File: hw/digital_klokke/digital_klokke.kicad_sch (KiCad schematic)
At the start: 8 parts, among them J101 Conn_01x02_Pin, SW101 SW_Push, SW102 SW_Push, SW103 SW_Push

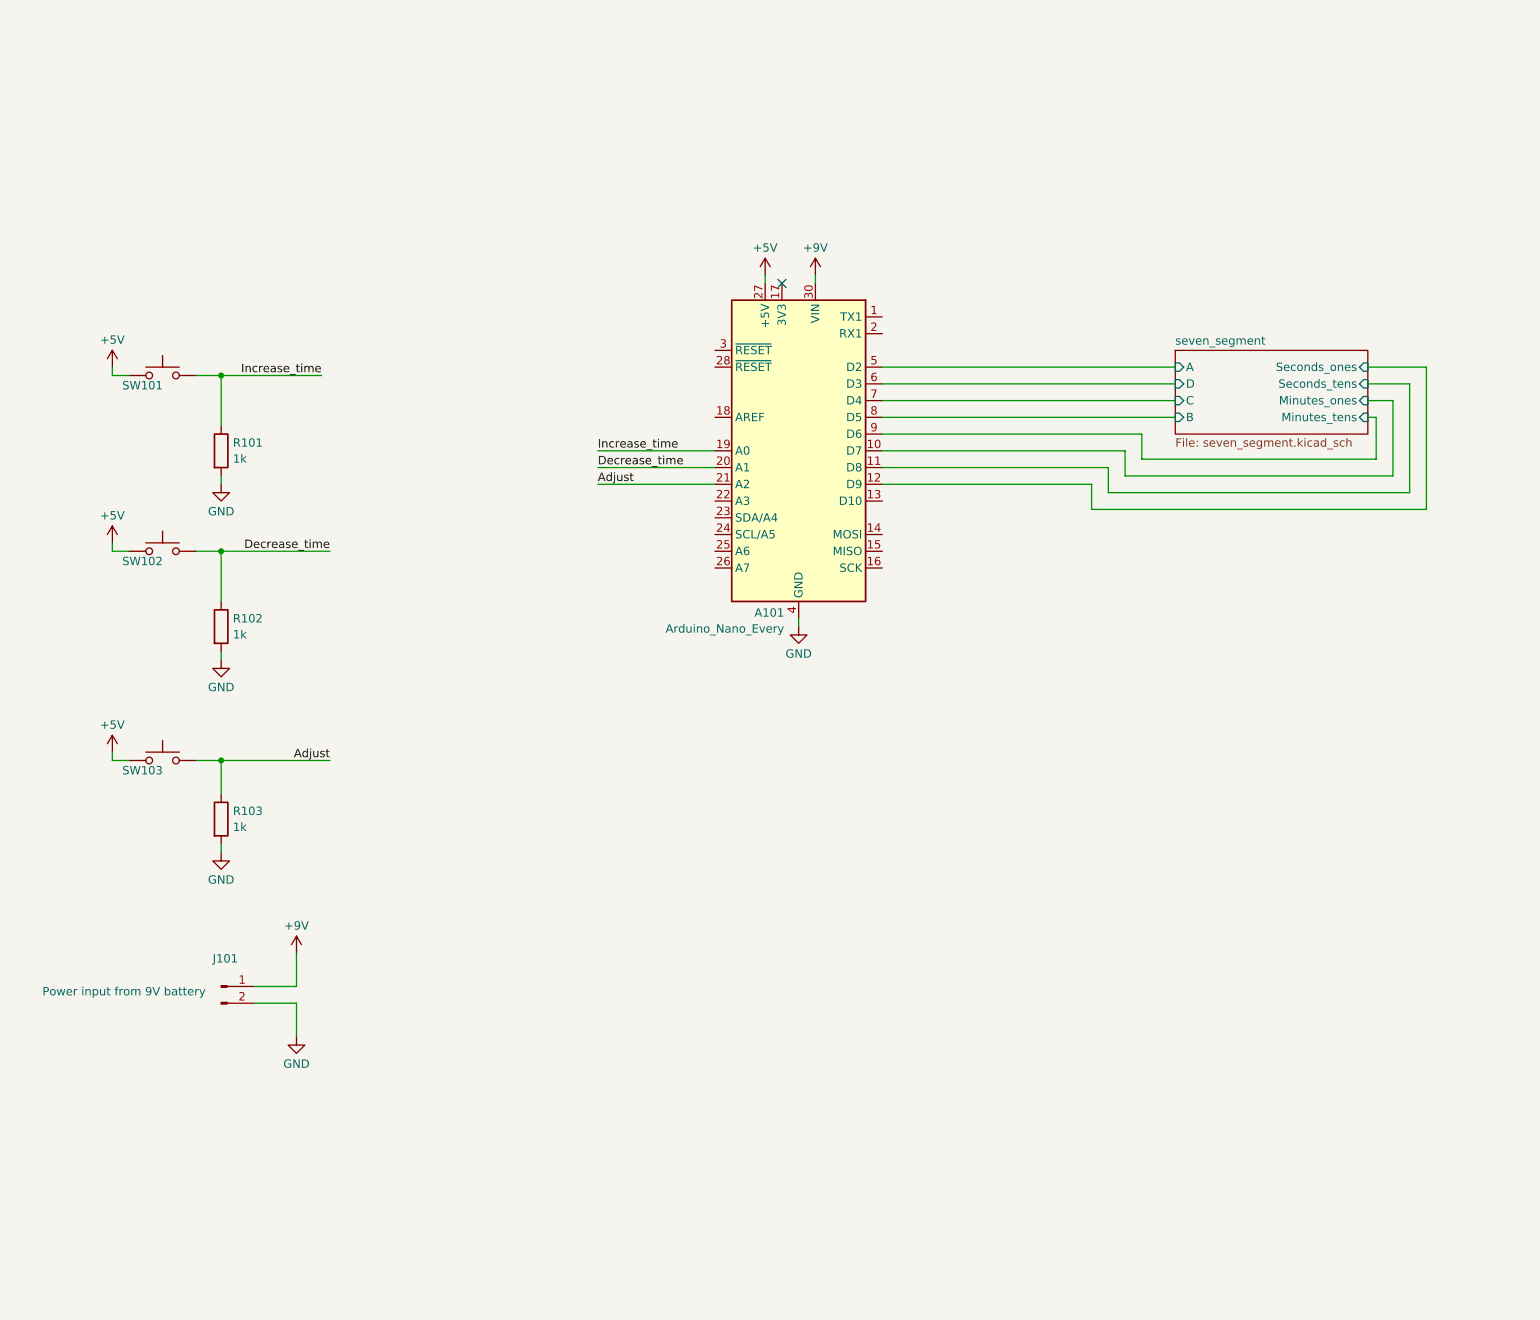
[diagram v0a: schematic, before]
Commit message: added led for power indication. Started routing
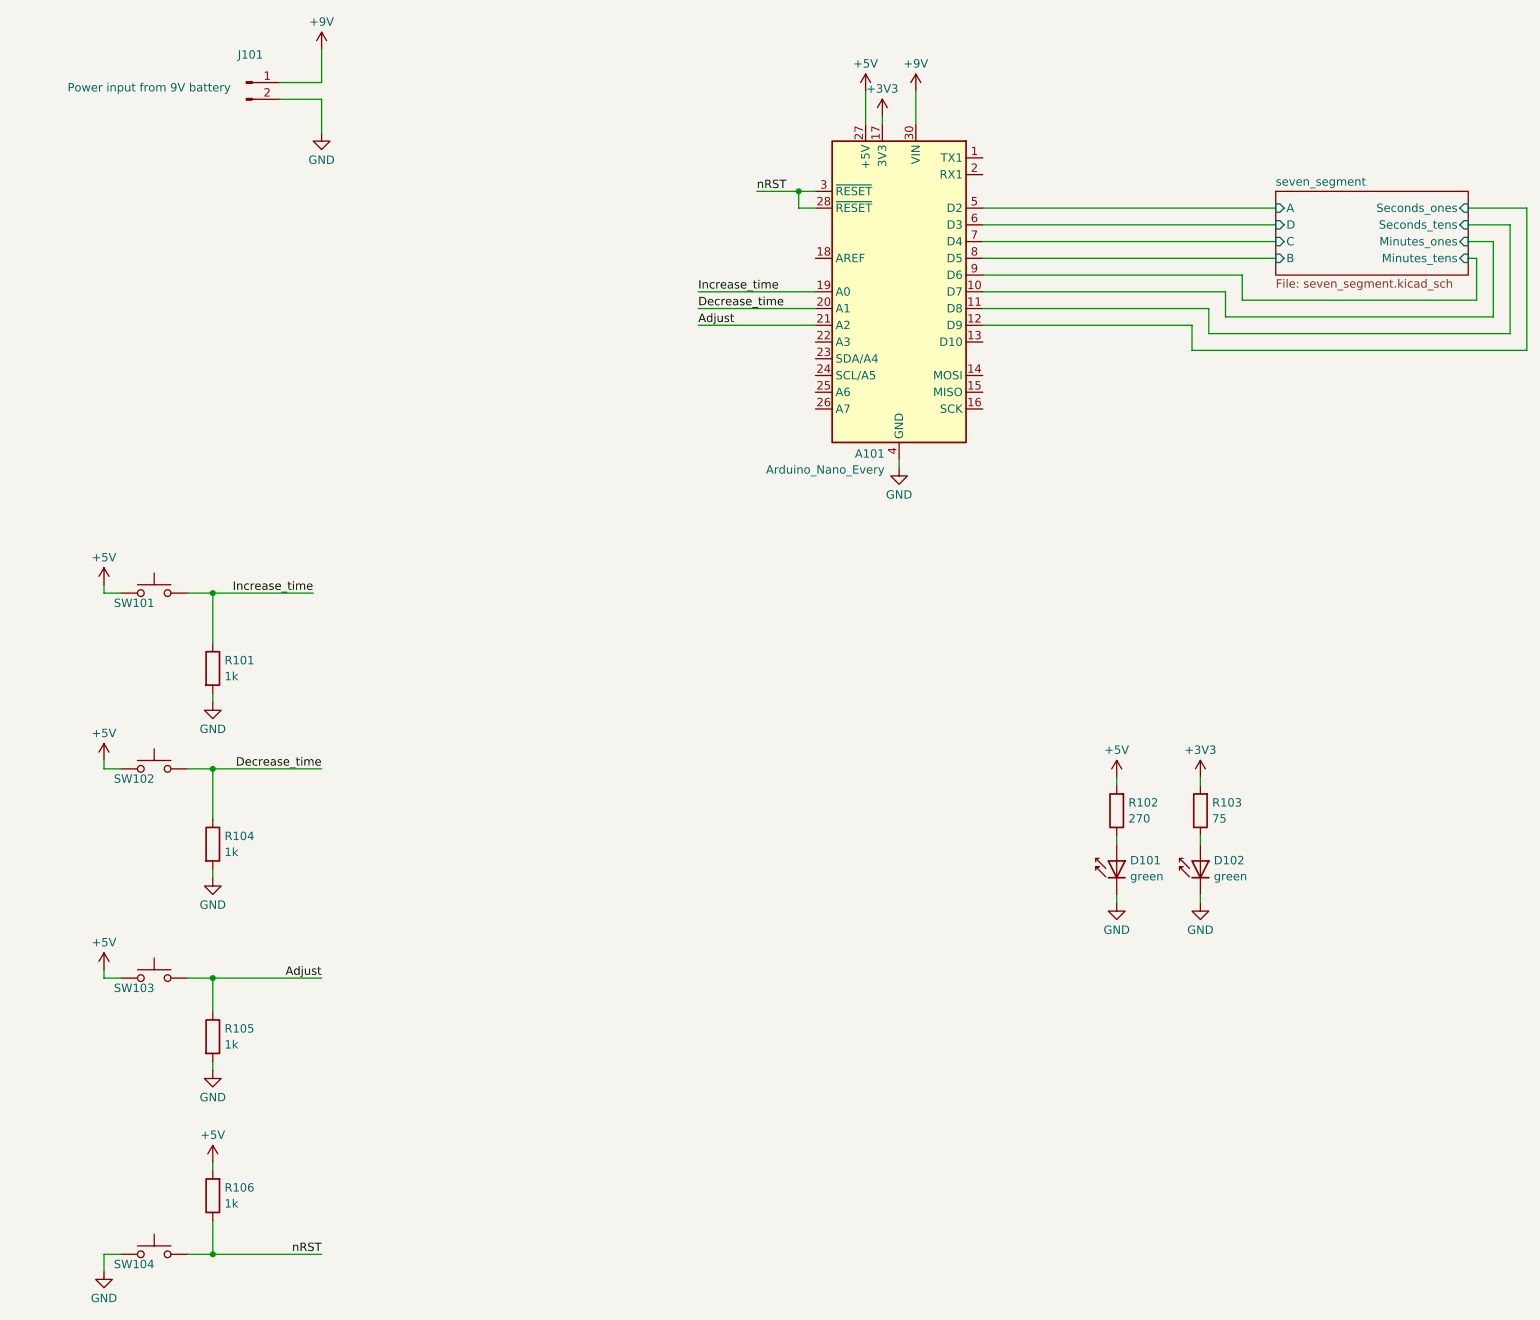
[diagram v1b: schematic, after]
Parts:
- added D101, D102: green, LED_THT:LED_D5.0mm, symbol LED:CQY99
- added R102: 270, Resistor_THT:R_Axial_DIN0207_L6.3mm_D2.5mm_P10.16mm_Horizontal, symbol Device:R
- added R103: 75, Resistor_THT:R_Axial_DIN0207_L6.3mm_D2.5mm_P10.16mm_Horizontal, symbol Device:R
- added R106: 1k, Resistor_THT:R_Axial_DIN0207_L6.3mm_D2.5mm_P10.16mm_Horizontal, symbol Device:R
- added SW104: SW_Push, OMG_Switches:SW_PUSH_1P1T_6x3.5mm_H5.0_APEM_MJTP1250, symbol Switch:SW_Push
- renumbered R102 to R104, R103 to R105
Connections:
- net +5V: now also R102.2, R106.2
- net GND: now also D101.1 (K), D102.1 (K), SW104.1
- net +3V3: now reaches A101.17 (3V3)
- net +3V3: now also R103.2
- net nRST: now reaches A101.28 (~{RESET})
- net nRST: now also A101.3 (~{RESET}), R106.1, SW104.2
- new net: D102.2 (A), R103.1
- new net: D101.2 (A), R102.1
- no-connect marks 1 -> 0
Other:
- moved on the sheet: A101, J101, R101, R104, R105, SW101, SW102, SW103

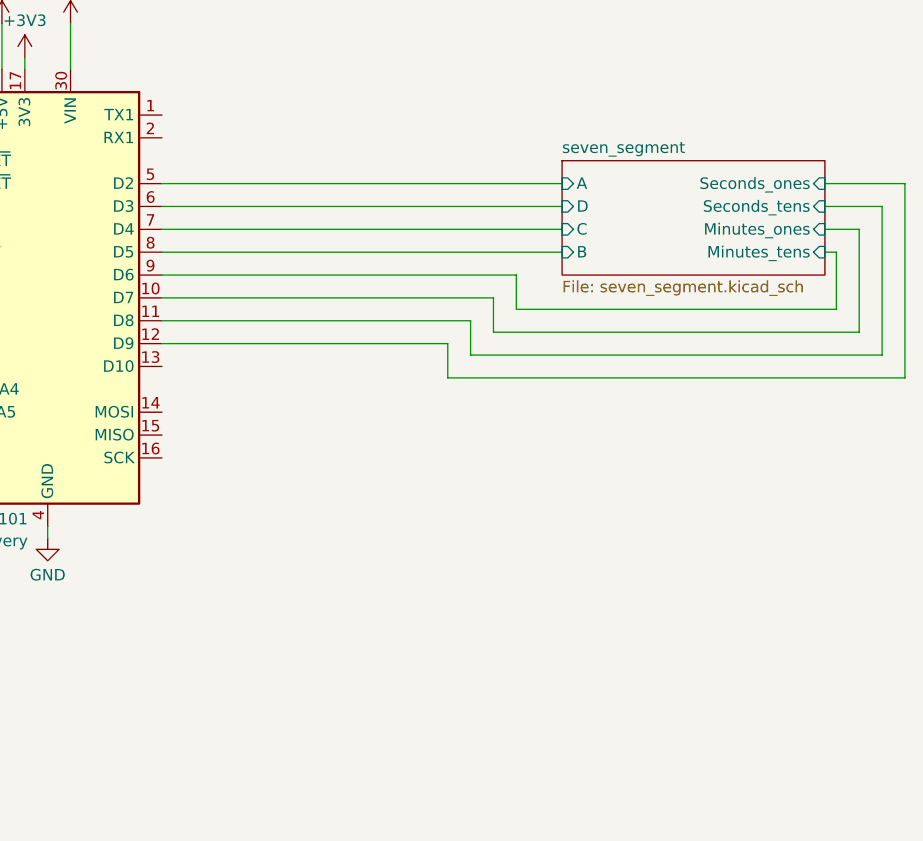
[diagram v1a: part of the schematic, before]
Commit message: added segment display footprint
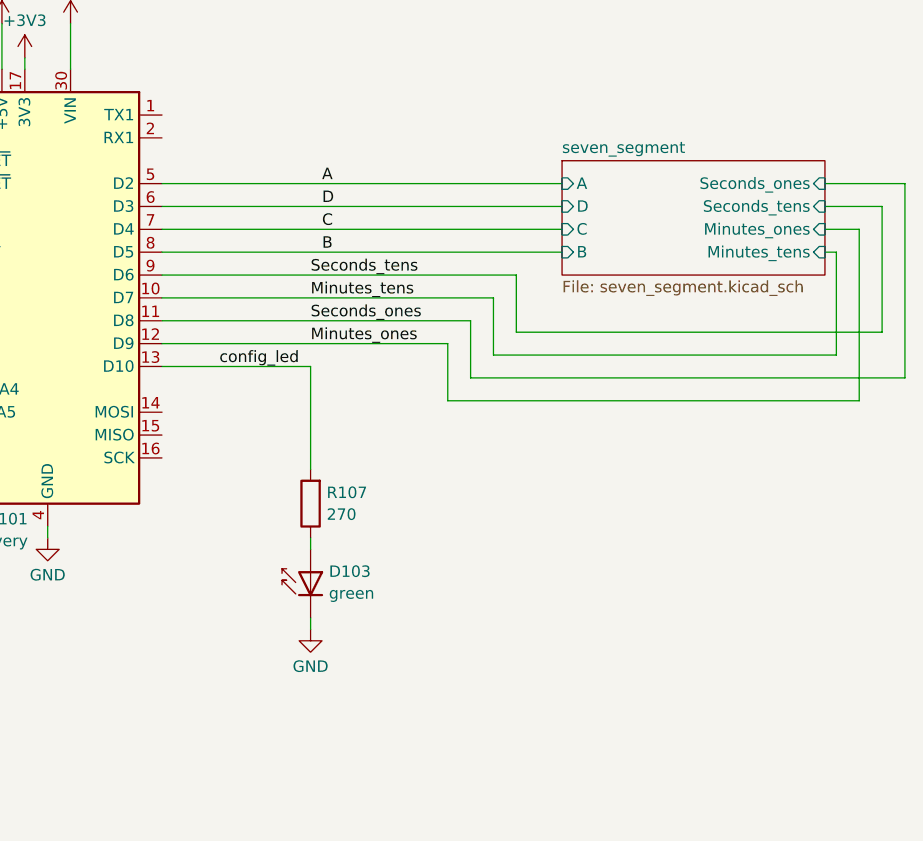
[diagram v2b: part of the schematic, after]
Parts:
- added D103: green, LED_THT:LED_D5.0mm, symbol LED:CQY99
- added R107: 270, Resistor_THT:R_Axial_DIN0207_L6.3mm_D2.5mm_P10.16mm_Horizontal, symbol Device:R
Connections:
- net GND: now also D103.1 (K)
- net config_led: now reaches A101.13 (D10)
- net config_led: now also R107.2
- net seven_segment/A renamed A
- net seven_segment/B renamed B
- net seven_segment/C renamed C
- net seven_segment/D renamed D
- net seven_segment/Minutes_ones renamed Minutes_tens
- net seven_segment/Minutes_tens renamed Seconds_tens
- net seven_segment/Seconds_ones renamed Minutes_ones
- net seven_segment/Seconds_tens renamed Seconds_ones
- new net: D103.2 (A), R107.1

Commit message: final design changes. Design freeze
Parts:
- removed D103: green, LED_THT:LED_D5.0mm, symbol LED:CQY99
- removed R107: 270, Resistor_THT:R_Axial_DIN0207_L6.3mm_D2.5mm_P10.16mm_Horizontal, symbol Device:R
- added H101, H102: MountingHole, MountingHole:MountingHole_4.3mm_M4, symbol Mechanical:MountingHole
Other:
- sheet seven_segment ports: added nDP; removed none
- company: (none) -> Noe Nonsens

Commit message: added resistor to each cathode
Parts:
- R101, R102, R103, R104, R105, R106: footprint Resistor_THT:R_Axial_DIN0207_L6.3mm_D2.5mm_P10.16mm_Horizontal -> Resistor_SMD:R_0805_2012Metric_Pad1.20x1.40mm_HandSolder
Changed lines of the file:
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@@
 			)
 		)
-		(property "Footprint" "Resistor_THT:R_Axial_DIN0207_L6.3mm_D2.5mm_P10.16mm_Horizontal"
+		(property "Footprint" "Resistor_SMD:R_0805_2012Metric_Pad1.20x1.40mm_HandSolder"
 			(at 68.072 142.24 90)
 			(effects
@@
 			)
 		)
-		(property "Footprint" "Resistor_THT:R_Axial_DIN0207_L6.3mm_D2.5mm_P10.16mm_Horizontal"
+		(property "Footprint" "Resistor_SMD:R_0805_2012Metric_Pad1.20x1.40mm_HandSolder"
 			(at 68.072 198.12 90)
 			(effects
@@
 			)
 		)
-		(property "Footprint" "Resistor_THT:R_Axial_DIN0207_L6.3mm_D2.5mm_P10.16mm_Horizontal"
+		(property "Footprint" "Resistor_SMD:R_0805_2012Metric_Pad1.20x1.40mm_HandSolder"
 			(at 71.628 222.25 90)
 			(effects
@@
 			)
 		)
-		(property "Footprint" "Resistor_THT:R_Axial_DIN0207_L6.3mm_D2.5mm_P10.16mm_Horizontal"
+		(property "Footprint" "Resistor_SMD:R_0805_2012Metric_Pad1.20x1.40mm_HandSolder"
 			(at 221.488 163.83 90)
 			(effects
@@
 			)
 		)
-		(property "Footprint" "Resistor_THT:R_Axial_DIN0207_L6.3mm_D2.5mm_P10.16mm_Horizontal"
+		(property "Footprint" "Resistor_SMD:R_0805_2012Metric_Pad1.20x1.40mm_HandSolder"
 			(at 68.072 168.91 90)
 			(effects
@@
 			)
 		)
-		(property "Footprint" "Resistor_THT:R_Axial_DIN0207_L6.3mm_D2.5mm_P10.16mm_Horizontal"
+		(property "Footprint" "Resistor_SMD:R_0805_2012Metric_Pad1.20x1.40mm_HandSolder"
 			(at 208.788 163.83 90)
 			(effects
